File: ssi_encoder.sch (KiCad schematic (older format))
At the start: 11 parts, among them Q2 BSS138, U2 ADM1491EBR

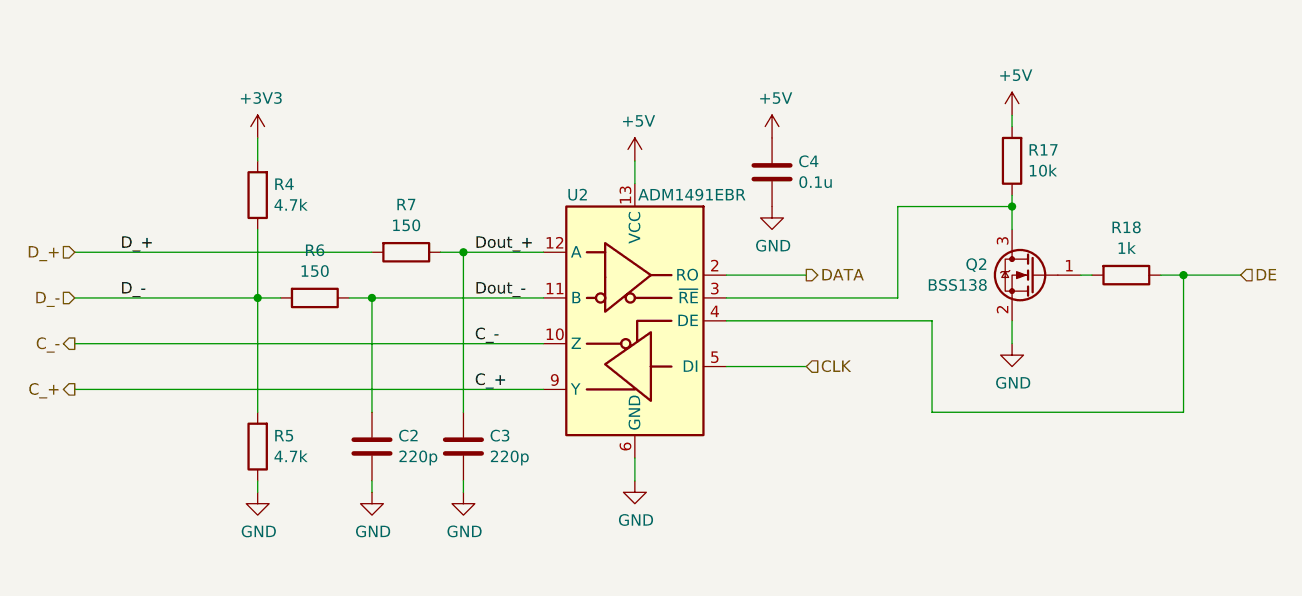
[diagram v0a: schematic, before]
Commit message: 見つけた設計ミスを全部反映
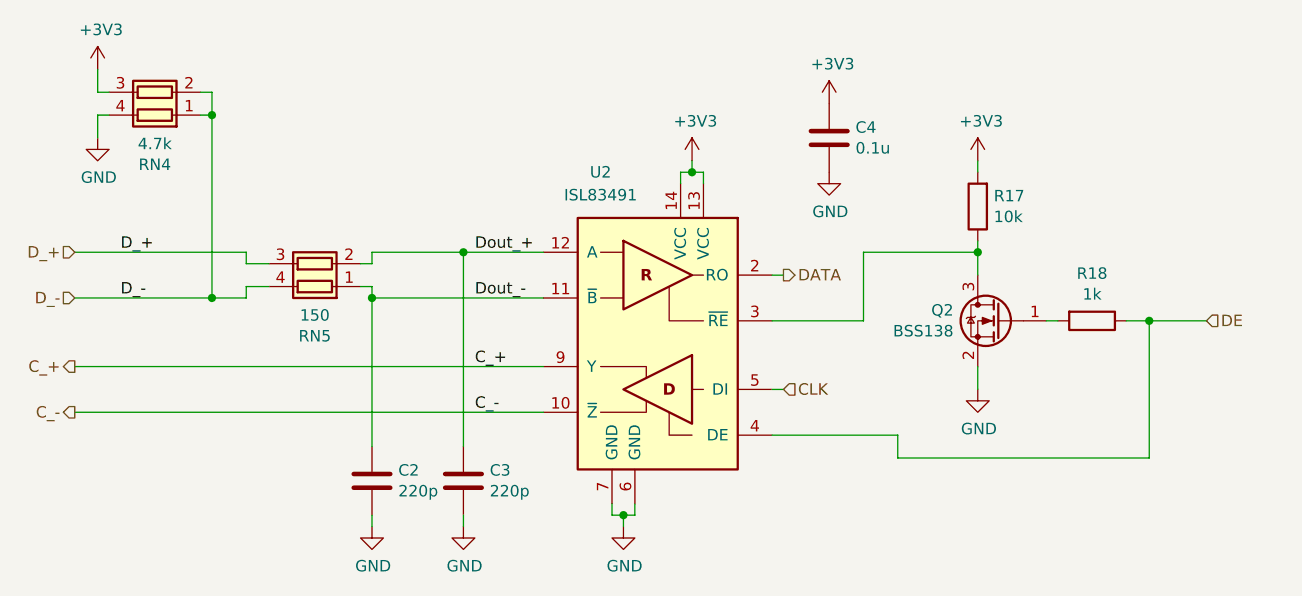
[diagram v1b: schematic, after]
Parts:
- removed R4, R5: 4.7k, Resistor_SMD:R_0603_1608Metric, symbol Device:R
- removed R6, R7: 150, Resistor_SMD:R_0603_1608Metric, symbol Device:R
- removed U2: ADM1491EBR, Package_SO:SOIC-14_3.9x8.7mm_P1.27mm, symbol Interface_UART:ADM1491EBR
- added RN4: 4.7k, Resistor_SMD:R_Array_Concave_2x0603, symbol Device:R_Pack02
- added RN5: 150, Resistor_SMD:R_Array_Concave_2x0603, symbol Device:R_Pack02
- added U2: ISL83491, Package_SO:SOIC-14_3.9x8.7mm_P1.27mm, symbol Interface_UART:ISL83491
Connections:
- net +5V is gone; now on net +3V3: C4.1, R17.2
- net +3V3: now also RN4.3 (R2.2), U2.13 (VCC), U2.14 (VCC)
- net CLK: now also U2.5 (DI)
- net C_+: now also U2.9 (Y)
- net C_-: now also U2.10 (~Z~)
- net DATA: now also U2.2 (RO)
- net DE: now also U2.4 (DE)
- net D_+: now also RN5.3 (R2.2)
- net D_-: now also RN4.1 (R1.1), RN4.2 (R2.1), RN5.4 (R1.2)
- net Dout_+: now also RN5.2 (R2.1), U2.12 (A)
- net Dout_-: now also RN5.1 (R1.1), U2.11 (~B)
- net GND: now also RN4.4 (R1.2), U2.6 (GND), U2.7 (GND)
- net at Q2.3 (D), R17.1: now also U2.3 (~RE)
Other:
- moved on the sheet: C2, C3, C4, Q2, R17, R18
